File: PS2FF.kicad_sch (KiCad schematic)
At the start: 11 parts, among them J1 PS2_SIDE, J2 DATA_RATE, J3 FF_SIDE, J4 POWER, SW1 DRIVE_TYPE, SW2 MEDIA_TYPE

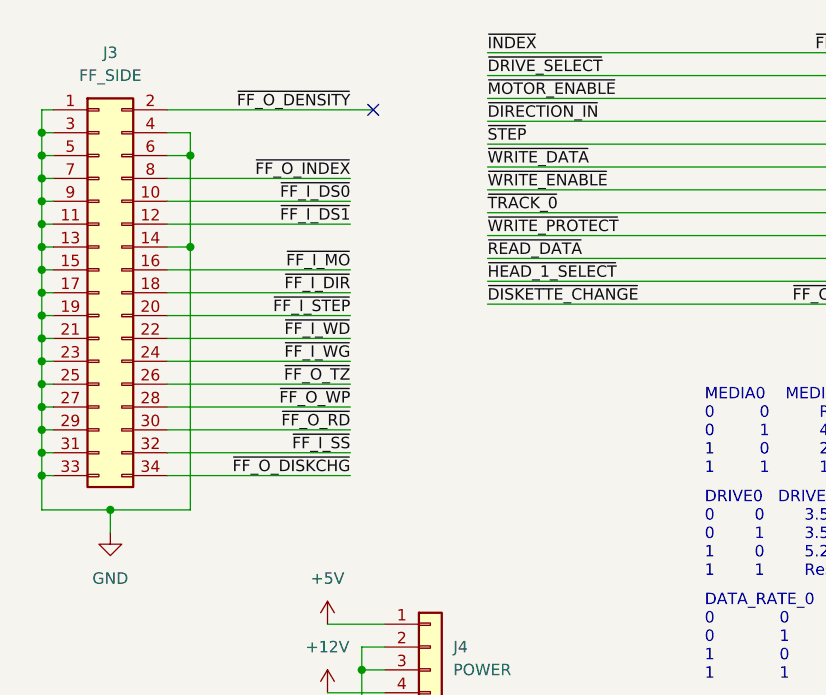
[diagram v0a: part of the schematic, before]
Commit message: Fix up some DRC errors in the schematic
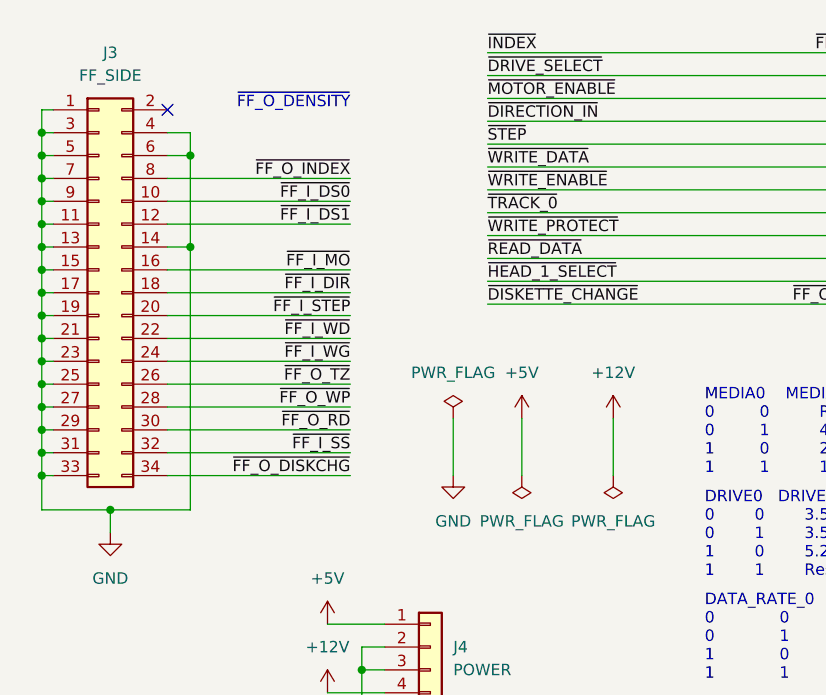
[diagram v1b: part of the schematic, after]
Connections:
- net ~{FF_O_DENSITY}: no longer names the net of J3.2 (Pin_2)
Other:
- note added: "~{FF_O_DENSITY}"
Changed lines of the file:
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@@
   (junction (at 83.82 63.5) (diameter 0) (color 0 0 0 0)
   )
-  (no_connect (at 120.65 25.4))
+  (no_connect (at 97.79 25.4))
   (wire (pts (xy 97.79 35.56) (xy 118.11 35.56))
     (stroke (width 0) (type default) (color 0 0 0 0))
@@
     (stroke (width 0) (type default) (color 0 0 0 0))
   )
-  (wire (pts (xy 97.79 25.4) (xy 120.65 25.4))
-    (stroke (width 0) (type default) (color 0 0 0 0))
-  )
   (wire (pts (xy 83.82 48.26) (xy 85.09 48.26))
     (stroke (width 0) (type default) (color 0 0 0 0))
@@
     (stroke (width 0) (type default) (color 0 0 0 0))
   )
+  (wire (pts (xy 147.32 59.69) (xy 147.32 66.04))
+    (stroke (width 0) (type default) (color 0 0 0 0))
+  )
   (wire (pts (xy 97.79 66.04) (xy 118.11 66.04))
     (stroke (width 0) (type default) (color 0 0 0 0))
@@
     (stroke (width 0) (type default) (color 0 0 0 0))
   )
+  (wire (pts (xy 129.54 59.69) (xy 129.54 66.04))
+    (stroke (width 0) (type default) (color 0 0 0 0))
+  )
   (wire (pts (xy 119.38 87.63) (xy 119.38 85.09))
     (stroke (width 0) (type default) (color 0 0 0 0))
@@
   )
   (wire (pts (xy 40.64 87.63) (xy 44.45 87.63))
+    (stroke (width 0) (type default) (color 0 0 0 0))
+  )
+  (wire (pts (xy 137.16 59.69) (xy 137.16 66.04))
     (stroke (width 0) (type default) (color 0 0 0 0))
   )
@@
     (effects (font (size 1.27 1.27)) (justify left bottom))
   )
+  (text "~{FF_O_DENSITY}" (at 118.11 25.4 180)
+    (effects (font (size 1.27 1.27)) (justify right bottom))
+  )
   (text "DATA_RATE_0   DATA_RATE_1\n0             0             500 kbps\n0             1             Reserved\n1             0             250 kbps\n1             1             1000 kbps"
     (at 157.48 88.9 0)
@@
   )
   (label "~{SECURITY_COMMAND}" (at 69.85 40.64 180)
-    (effects (font (size 1.27 1.27)) (justify right bottom))
-  )
-  (label "~{FF_O_DENSITY}" (at 118.11 25.4 180)
     (effects (font (size 1.27 1.27)) (justify right bottom))
   )
@@
     (pin "4")
   )
+  (symbol (lib_id "power:+12V") (at 147.32 59.69 0) (unit 1)
+    (in_bom yes) (on_board yes) (fields_autoplaced)
+    (property "Reference" "#PWR0103" (id 0) (at 147.32 63.5 0)
+      (effects (font (size 1.27 1.27)) hide)
+    )
+    (property "Value" "+12V" (id 1) (at 147.32 54.61 0))
+    (property "Footprint" "" (id 2) (at 147.32 59.69 0)
+      (effects (font (size 1.27 1.27)) hide)
+    )
+    (property "Datasheet" "" (id 3) (at 147.32 59.69 0)
+      (effects (font (size 1.27 1.27)) hide)
+    )
+    (pin "1")
+  )
   (symbol (lib_id "Connector_Generic:Conn_01x04") (at 127 85.09 0) (unit 1)
     (in_bom yes) (on_board yes) (fields_autoplaced)
@@
     (pin "3")
   )
+  (symbol (lib_id "power:PWR_FLAG") (at 129.54 59.69 0) (unit 1)
+    (in_bom yes) (on_board yes) (fields_autoplaced)
+    (property "Reference" "#FLG0101" (id 0) (at 129.54 57.785 0)
+      (effects (font (size 1.27 1.27)) hide)
+    )
+    (property "Value" "PWR_FLAG" (id 1) (at 129.54 54.61 0))
+    (property "Footprint" "" (id 2) (at 129.54 59.69 0)
+      (effects (font (size 1.27 1.27)) hide)
+    )
+    (property "Datasheet" "~" (id 3) (at 129.54 59.69 0)
+      (effects (font (size 1.27 1.27)) hide)
+    )
+    (pin "1")
+  )
+  (symbol (lib_id "power:PWR_FLAG") (at 147.32 66.04 180) (unit 1)
+    (in_bom yes) (on_board yes) (fields_autoplaced)
+    (property "Reference" "#FLG0103" (id 0) (at 147.32 67.945 0)
+      (effects (font (size 1.27 1.27)) hide)
+    )
+    (property "Value" "PWR_FLAG" (id 1) (at 147.32 71.12 0))
+    (property "Footprint" "" (id 2) (at 147.32 66.04 0)
+      (effects (font (size 1.27 1.27)) hide)
+    )
+    (property "Datasheet" "~" (id 3) (at 147.32 66.04 0)
+      (effects (font (size 1.27 1.27)) hide)
+    )
+    (pin "1")
+  )
+  (symbol (lib_id "power:GND") (at 129.54 66.04 0) (unit 1)
+    (in_bom yes) (on_board yes) (fields_autoplaced)
+    (property "Reference" "#PWR0102" (id 0) (at 129.54 72.39 0)
+      (effects (font (size 1.27 1.27)) hide)
+    )
+    (property "Value" "GND" (id 1) (at 129.54 71.12 0))
+    (property "Footprint" "" (id 2) (at 129.54 66.04 0)
+      (effects (font (size 1.27 1.27)) hide)
+    )
+    (property "Datasheet" "" (id 3) (at 129.54 66.04 0)
+      (effects (font (size 1.27 1.27)) hide)
+    )
+    (pin "1")
+  )
   (symbol (lib_id "Device:R_Small_US") (at 48.26 92.71 180) (unit 1)
     (in_bom yes) (on_board yes)
@@
     (pin "1")
   )
+  (symbol (lib_id "power:PWR_FLAG") (at 137.16 66.04 180) (unit 1)
+    (in_bom yes) (on_board yes) (fields_autoplaced)
+    (property "Reference" "#FLG0102" (id 0) (at 137.16 67.945 0)
+      (effects (font (size 1.27 1.27)) hide)
+    )
+    (property "Value" "PWR_FLAG" (id 1) (at 137.16 71.12 0))
+    (property "Footprint" "" (id 2) (at 137.16 66.04 0)
+      (effects (font (size 1.27 1.27)) hide)
+    )
+    (property "Datasheet" "~" (id 3) (at 137.16 66.04 0)
+      (effects (font (size 1.27 1.27)) hide)
+    )
+    (pin "1")
+  )
   (symbol (lib_id "Device:R_Small_US") (at 40.64 92.71 180) (unit 1)
     (in_bom yes) (on_board yes)
@@
     (pin "1")
     (pin "2")
+  )
+  (symbol (lib_id "power:+5V") (at 137.16 59.69 0) (unit 1)
+    (in_bom yes) (on_board yes)
+    (property "Reference" "#PWR0101" (id 0) (at 137.16 63.5 0)
+      (effects (font (size 1.27 1.27)) hide)
+    )
+    (property "Value" "+5V" (id 1) (at 137.16 54.61 0))
+    (property "Footprint" "" (id 2) (at 137.16 59.69 0)
+      (effects (font (size 1.27 1.27)) hide)
+    )
+    (property "Datasheet" "" (id 3) (at 137.16 59.69 0)
+      (effects (font (size 1.27 1.27)) hide)
+    )
+    (pin "1")
   )
   (symbol (lib_id "Connector_Generic:Conn_02x17_Odd_Even") (at 90.17 45.72 0) (unit 1)
@@
   )
   (symbol_instances
+    (path "/b224d8e5-aec9-4e03-b5ab-45047148f6be"
+      (reference "#FLG0101") (unit 1) (value "PWR_FLAG") (footprint "")
+    )
+    (path "/e15d61d5-47f6-490b-a5e2-187515a03b1c"
+      (reference "#FLG0102") (unit 1) (value "PWR_FLAG") (footprint "")
+    )
+    (path "/cbcfa087-cca8-4faa-9d62-22fd4d6662d2"
+      (reference "#FLG0103") (unit 1) (value "PWR_FLAG") (footprint "")
+    )
     (path "/debe3c1f-d15b-4a2f-85b1-4872c7c0b7b0"
       (reference "#PWR01") (unit 1) (value "+5V") (footprint "")
@@
       (reference "#PWR08") (unit 1) (value "GND") (footprint "")
     )
+    (path "/f6829c47-36c1-459e-84ae-44474415497c"
+      (reference "#PWR0101") (unit 1) (value "+5V") (footprint "")
+    )
+    (path "/cbe7f874-6f7c-49cf-84a9-351a57351808"
+      (reference "#PWR0102") (unit 1) (value "GND") (footprint "")
+    )
+    (path "/6ec6d6bd-7bba-417a-9953-9f445c5151ec"
+      (reference "#PWR0103") (unit 1) (value "+12V") (footprint "")
+    )
     (path "/37916126-962b-4377-93b5-94580b9bf264"

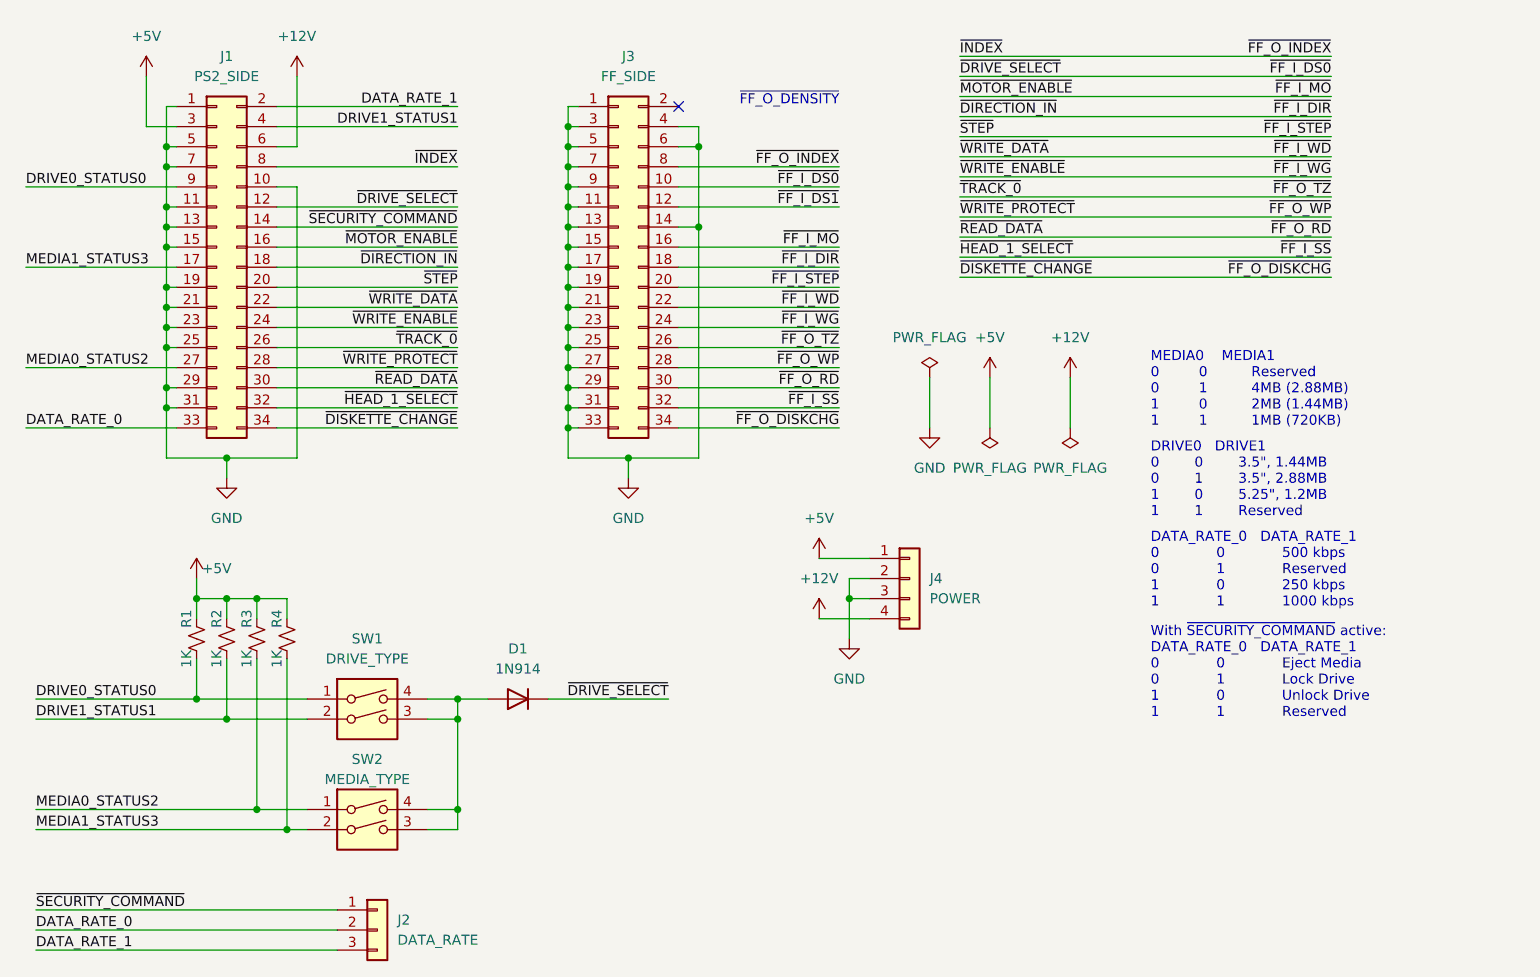
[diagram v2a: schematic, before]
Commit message: automate things: Swap to using a buffer to automate
  - Use a simple buffer to drive outputs to the host side.
  - Wire in FF_O_DENSITY to the appropriate pin via the buffers.
    Note: this requires FF to be set to invert this output!
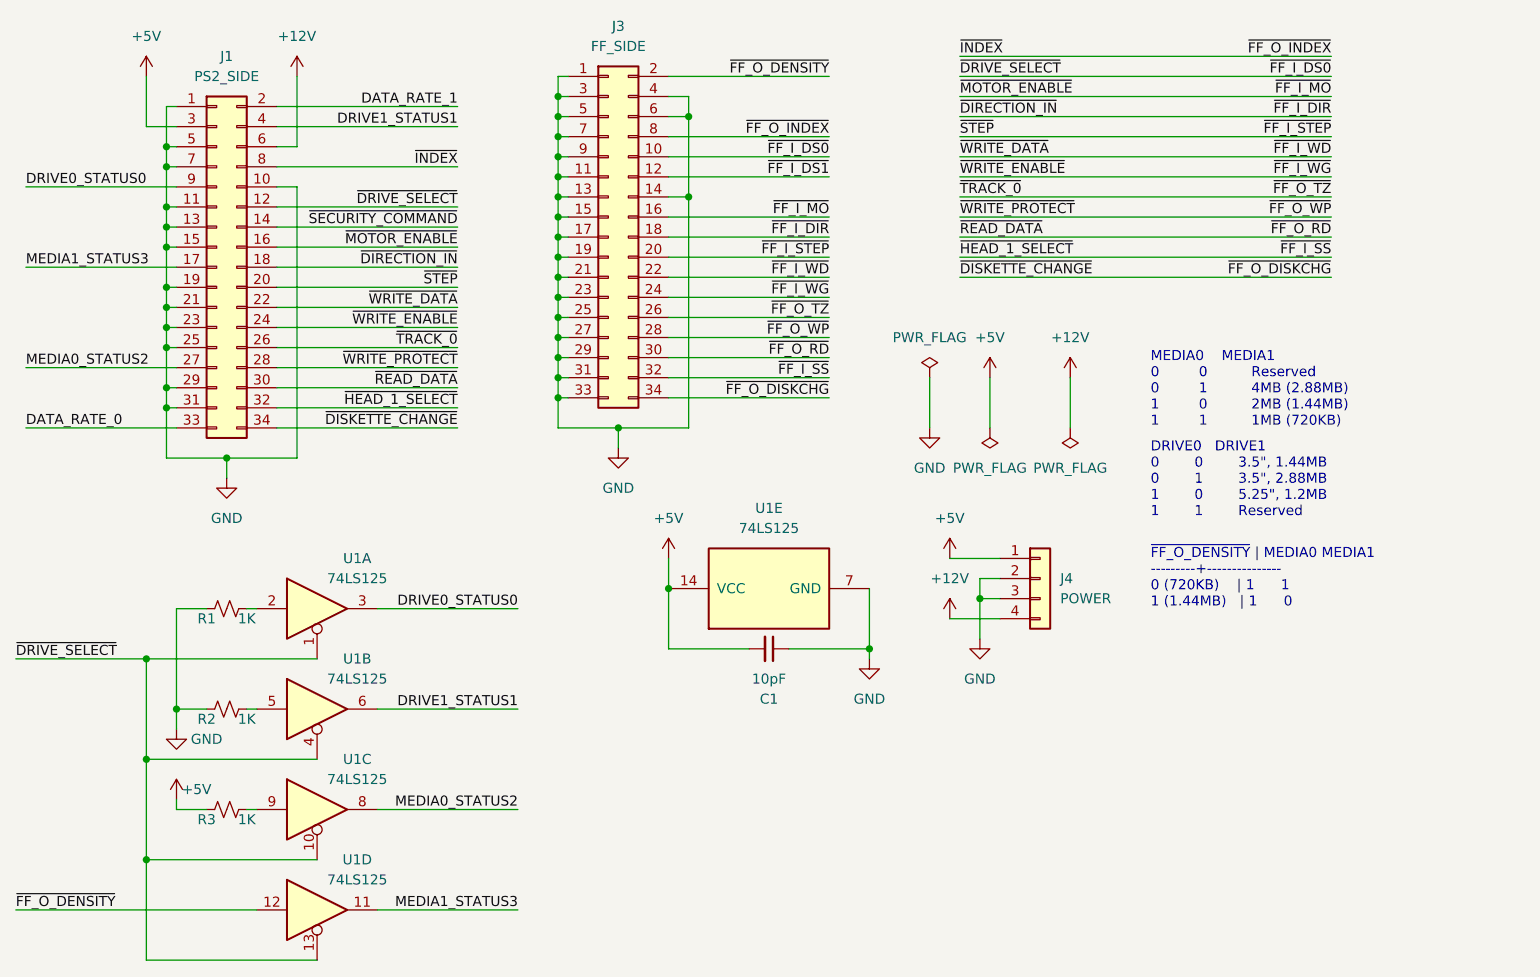
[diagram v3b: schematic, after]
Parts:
- removed D1: 1N914, Diode_THT:D_DO-35_SOD27_P7.62mm_Horizontal, symbol Diode:1N914
- removed J2: DATA_RATE, Connector_PinHeader_2.54mm:PinHeader_1x03_P2.54mm_Vertical, symbol Connector_Generic:Conn_01x03
- removed R4: 1K, Resistor_SMD:R_0805_2012Metric, symbol Device:R_Small_US
- removed SW1: DRIVE_TYPE, Button_Switch_THT:SW_DIP_SPSTx02_Piano_10.8x6.64mm_W7.62mm_P2.54mm, symbol Switch:SW_DIP_x02
- removed SW2: MEDIA_TYPE, Button_Switch_THT:SW_DIP_SPSTx02_Piano_10.8x6.64mm_W7.62mm_P2.54mm, symbol Switch:SW_DIP_x02
- added C1: 10pF, Capacitor_SMD:C_0805_2012Metric_Pad1.18x1.45mm_HandSolder, symbol Device:C_Small
- added U1: 74LS125, Package_SO:SOIC-14_3.9x8.7mm_P1.27mm, symbol 74xx:74LS125
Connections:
- net +5V: now also C1.2, U1.14 (VCC); no longer R1.2, R2.2
- net DRIVE0_STATUS0: now also U1.3; no longer R1.1
- net DRIVE1_STATUS1: now also U1.6; no longer R2.1
- net GND: now also R1.2, R2.2, C1.1, U1.7 (GND)
- net MEDIA0_STATUS2: now also U1.8; no longer R3.1
- net MEDIA1_STATUS3: now also U1.11
- net ~{DRIVE_SELECT}: now also U1.1, U1.10, U1.13, U1.4
- net ~{FF_O_DENSITY}: now reaches J3.2 (Pin_2)
- net ~{FF_O_DENSITY}: now also U1.12
- new net: R1.1, U1.2
- new net: R3.1, U1.9
- new net: R2.1, U1.5
- no-connect marks 1 -> 0
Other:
- note added: "~{FF_O_DENSITY} | MEDIA0 MEDIA1 ---------+--------------- 0 (720KB) | 1 1 1 (1.44MB) | 1 0"
- note removed: "DATA_RATE_0 DATA_RATE_1 0 0 500 kbps 0 1 Reserved 1 0 250 kbps 1 1 1000 kbps"
- note removed: "With ~{SECURITY_COMMAND} active: DATA_RATE_0 DATA_RATE_1 0 0 Eject Media 0 1 Lock Drive 1 0 Unlock Drive 1 1 Reserved"
- note removed: "~{FF_O_DENSITY}"
- moved on the sheet: J3, J4
